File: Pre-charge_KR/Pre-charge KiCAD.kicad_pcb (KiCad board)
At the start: 2 copper layers, 62.9 x 86.1 mm, 60 parts, among them IC1 AL5890-10D-13, IC2 TLV1701AIDBVT, J1 Conn_01x02, J2 Conn_01x06, J3 Conn_01x02, J4 Conn_01x02, K2 G5Q-1A4-DC12, K3 67-1-A-12/2D, Q1 2N7000, Q2 2N7000, Q4 2N7000, U1 HCPL-817-000E, U10 LM7805MPX/NOPB, U13 HCPL-817-000E, U2 LM339N/NOPB, U3 SN74AHCT1G08DBVR, U7 LM741CN/NOPB, U8 SN74AHC1G04DBVRE4

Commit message: precharge complete
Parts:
- removed C11: 0.1uF, FA14_Capacitor:FA18X7R1H104KNU00
- removed C7: 0.22uF, FA14_Capacitor:FA14X7R1H224KNU00
- removed IC1: AL5890-10D-13, AL589010D13:AL589010D13
- removed LED1: LTL-1CHG, LTL1CHG:LTL1CHG
- removed Q1: 2N7000, Package_TO_SOT_THT:TO-92_Inline
- removed R12: 20k, Resistor_THT:R_Axial_DIN0207_L6.3mm_D2.5mm_P10.16mm_Horizontal
- removed R24: 1M, Resistor_THT:R_Axial_DIN0207_L6.3mm_D2.5mm_P10.16mm_Horizontal
- removed R36: 6.8k, Resistor_THT:R_Axial_DIN0207_L6.3mm_D2.5mm_P10.16mm_Horizontal
- removed R37: 4.7k, Resistor_THT:R_Axial_DIN0207_L6.3mm_D2.5mm_P10.16mm_Horizontal
- removed the REF** at (97.4, 35.8)
- removed the REF** at (44.7, 111.9)
- removed the REF** at (97.5, 111.7)
- removed the REF** at (44.6, 35.7)
- removed U10: LM7805MPX/NOPB, Package_TO_SOT_SMD:SOT-223-3_TabPin2
- removed U3: SN74AHCT1G08DBVR, Package_TO_SOT_SMD:SOT-23-5
- removed U7: LM741CN/NOPB, Package_DIP:DIP-8_W7.62mm
- added C5: 2.2uF, FA14_Capacitor:FA14X7R1H224KNU00, F.Cu at (100.9, 70.7)
- added D2: 1N4148, Diode_THT:D_DO-35_SOD27_P7.62mm_Horizontal, F.Cu at (79.9, 57.3)
- added IC3: SN74LVC1G11DCKRE4, SOT65:SOT65P210X110-6N, F.Cu at (85.2, 51.9)
- added IC4: SN74LVC1G08IDCKRQ1, AND:SOT65P210X110-5N, F.Cu at (85.2, 54.9)
- added R10: 56k, Resistor_THT:R_Axial_DIN0411_L9.9mm_D3.6mm_P12.70mm_Horizontal, F.Cu at (76.9, 33.3)
- added R3: 100k, Resistor_THT:R_Axial_DIN0207_L6.3mm_D2.5mm_P10.16mm_Horizontal, F.Cu at (89.4, 52.0)
- added R6: 100k, Resistor_THT:R_Axial_DIN0207_L6.3mm_D2.5mm_P10.16mm_Horizontal, F.Cu at (99.5, 66.1)
- added REF**: MountingHole_3.2mm_M3, MountingHole:MountingHole_3.2mm_M3, F.Cu at (108.2, 86.7)
- added REF**: MountingHole_3.2mm_M3, MountingHole:MountingHole_3.2mm_M3, F.Cu at (108.2, 34.3)
- added REF**: MountingHole_3.2mm_M3, MountingHole:MountingHole_3.2mm_M3, F.Cu at (34.3, 86.7)
- added REF**: MountingHole_3.2mm_M3, MountingHole:MountingHole_3.2mm_M3, F.Cu at (34.2, 34.3)
- C1, C4: value 0.1uF -> 1uF
- C2: value 10uF -> 0.1uF; footprint Capacitor_THT:CP_Radial_D5.0mm_P2.50mm -> FA14_Capacitor:FA18X7R1H104KNU00
- D1: value TZX3V9C-TAP -> 1N4001; footprint Diode_THT:D_DO-35_SOD27_P7.62mm_Horizontal -> Diode_THT:D_DO-41_SOD81_P10.16mm_Horizontal
- D3: value TZX3V0B-TR -> 1N4148
- J3: footprint Phoenix 1x2 Connector:Phoenix_1x2_1729128 -> Connector_JST:JST_XH_B2B-XH-A_1x02_P2.50mm_Vertical
- R1: value 1.5k -> 100k
- R11: value 10k -> 330
- R2: value 1.5k -> 1M
- R32, R33, R7: value 10k -> 100k
- R34: value 180k -> 1.8M
- R35: value 1k -> 2.2k
- R4: value 6.8k -> 10k
- R5: value 4.7k -> 27k
- R8: value 10k -> 56k; footprint Resistor_THT:R_Axial_DIN0207_L6.3mm_D2.5mm_P10.16mm_Horizontal -> Resistor_THT:R_Axial_DIN0411_L9.9mm_D3.6mm_P12.70mm_Horizontal
- R9: value 100 -> 56k; footprint Resistor_THT:R_Axial_DIN0207_L6.3mm_D2.5mm_P10.16mm_Horizontal -> Resistor_THT:R_Axial_DIN0411_L9.9mm_D3.6mm_P12.70mm_Horizontal
- U2: value LM339N/NOPB -> MCP1703AT-3302E/MBVAO; footprint LM339N:DIP794W53P254L1930H508Q14N -> Package_TO_SOT_SMD:SOT-89-3
- U8: value SN74AHC1G04DBVRE4 -> SN74LVC1G04QDBVRQ1
- moved U1 82.8 mm to (105.4, 41.0), turned to -90 degrees
- moved J3 72.4 mm to (43.1, 51.0)
- moved R2 72.3 mm to (46.2, 88.5), turned to 0 degrees
- moved R9 62.4 mm to (65.4, 33.6)
- moved R29 62.2 mm to (92.8, 85.0), turned to 0 degrees
- moved C3 59.9 mm to (40.7, 63.5), turned to 0 degrees
- moved R33 57.6 mm to (102.9, 78.3), turned to 180 degrees
- moved R11 57.4 mm to (76.4, 37.7)
- moved Q2 56.8 mm to (43.2, 58.8), turned to 180 degrees
- moved U13 51.0 mm to (86.4, 78.9), turned to 90 degrees
- moved R27 50.8 mm to (47.0, 71.4)
- moved PS1 49.6 mm to (43.1, 68.3), turned to -90 degrees
- moved R32 48.1 mm to (92.8, 81.7), turned to 0 degrees
- moved R28 45.1 mm to (76.8, 83.1), turned to 0 degrees
- moved C4 45.0 mm to (47.4, 49.5), turned to 0 degrees
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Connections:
- C1 pad 1: 12V_HV -> 3.3V
- C1 pad 2: TS- -> GLV-
- C10 pad 1: 5V -> 3.3V
- C14 pad 1: 5V -> 3.3V
- C2 pad 1: Precharge NOT done -> 3.3V
- C4 pad 1: GLV- -> GLV+
- C4 pad 2: GLV+ -> GLV-
- D1 pad 1: 3V9 -> SDWN_PC
- D1 pad 2: GLV- -> Net-(D1-A)
- D3 pad 1: 3Vref -> Net-(D3-K)
- D3 pad 2: GLV- -> TS-
- J2 pad 1: Precharge_ON -> Shutdown_AIR1+
- J2 pad 3: Shutdown_AIR1+ -> GLV-
- J2 pad 4: Precharge_done/Close_AIR1 -> Precharge_done
- J2 pad 5: TS_activate -> Precharge_EN
- J2 pad 6: GLV- -> Precharge_ON
- K3 pad 3: Net-(Q4-D) -> Net-(D1-A)
- Q4 pad 2: Precharge NOT done -> Net-(D2-K)
- Q4 pad 3: Net-(Q4-D) -> Net-(D1-A)
- R1 pad 1: GLV+ -> GLV-
- R1 pad 2: 3V9 -> Precharge_done
- R11 pad 1: Net-(Q1-G) -> Net-(D3-K)
- R11 pad 2: Precharge_done/Close_AIR1 -> Net-(R10-Pad2)
- R13 pad 2: Net-(R12-Pad1) -> Net-(IC3-B)
- R2 pad 1: GLV+ -> Net-(IC2-IN+)
- R2 pad 2: 3Vref -> Net-(IC2-OUT)
- R28 pad 2: Net-(U7-+) -> Net-(R28-Pad2)
- R29 pad 1: Net-(U7-+) -> Net-(R28-Pad2)
- R30 pad 2: Net-(IC2-IN+) -> Net-(IC2-IN-)
- R31 pad 1: Net-(IC2-IN+) -> Net-(IC2-IN-)
- R32 pad 1: Net-(U7--) -> Net-(R28-Pad2)
- R32 pad 2: Net-(IC2-IN-) -> Net-(IC2-IN+)
- R33 pad 1: Net-(IC2-IN-) -> Net-(IC2-IN+)
- R35 pad 1: Net-(IC2-OUT) -> Net-(R35-Pad1)
- R4 pad 1: Net-(R4-Pad1) -> Net-(IC2-OUT)
- R4 pad 2: Net-(U2A-+) -> 12V_HV
- R5 pad 1: Net-(U2A-+) -> Net-(IC3-B)
- R5 pad 2: GLV- -> SDWN_PC
- R7 pad 1: Precharge_ON -> GLV-
- R7 pad 2: 3V9 -> Net-(D2-K)
- R8 pad 1: Net-(Q1-D) -> PRE_RESIST+
- R8 pad 2: 3V9 -> Net-(R8-Pad2)
- R9 pad 1: Net-(Q1-G) -> Net-(R8-Pad2)
- R9 pad 2: TS_activate -> Net-(R10-Pad1)
- U1 pad 1: Net-(LED1-K) -> Net-(D3-K)
- U1 pad 2: Net-(IC1-IN) -> TS-
- U1 pad 3: Net-(R4-Pad1) -> Precharge_ON
- U1 pad 4: GLV+ -> 3.3V
- U13 pad 1: Net-(IC2-OUT) -> Net-(R35-Pad1)
- U13 pad 2: TS- -> Net-(IC2-OUT)
- U13 pad 3: Net-(R36-Pad2) -> Precharge_done
- U13 pad 4: GLV+ -> 3.3V
- U2 pad 2: Precharge_ON -> GLV+
- U2 pad 3: GLV+ -> 3.3V
- U8 pad 2: Precharge_done/Close_AIR1 -> Precharge_done
- U8 pad 4: Net-(R24-Pad1) -> Precharge NOT done
- U8 pad 5: 5V -> 3.3V
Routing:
- net TS+: track 20.6 -> 144.8 mm
- net GLV+: track 170.2 -> 52.0 mm, vias 1 -> 0
- net TS-: track 49.2 -> 149.3 mm
- net 3.3V: track 0.00 -> 93.9 mm, vias 0 -> 1
- net PRE_RESIST+: track 28.4 -> 113.5 mm
- net Precharge_done/Close_AIR1: track 66.8 -> 0.00 mm, vias 1 -> 0
- net Precharge_ON: track 61.5 -> 9.76 mm, vias 1 -> 0
- net Net-(Q1-D): track 49.8 -> 0.00 mm
- net Net-(R12-Pad1): track 49.6 -> 0.00 mm, vias 1 -> 0
- net 5V: track 49.2 -> 0.00 mm, vias 1 -> 0
- net Net-(IC2-IN+): track 23.3 -> 70.5 mm, vias 0 -> 1
- net Net-(R4-Pad1): track 41.1 -> 0.00 mm
- net Precharge_done: track 0.00 -> 40.3 mm, vias 0 -> 1
- net GLV-: track 39.5 -> 0.00 mm
- net Net-(D2-K): track 0.00 -> 39.1 mm, vias 0 -> 1
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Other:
- board size 62.9 x 86.1 mm -> 88.7 x 61.1 mm
- board text added: "HV"
- board text added: "LV"

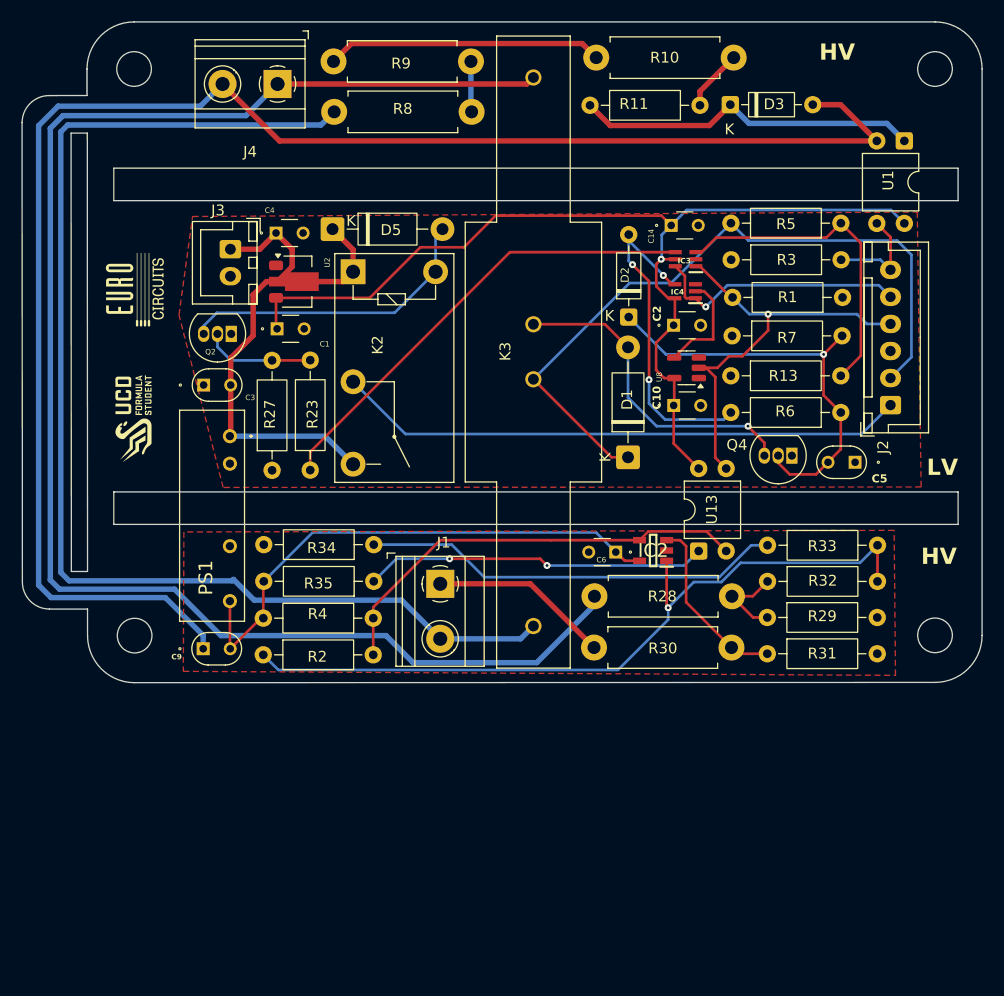
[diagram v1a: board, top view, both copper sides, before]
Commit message: precharge and discharge fixed
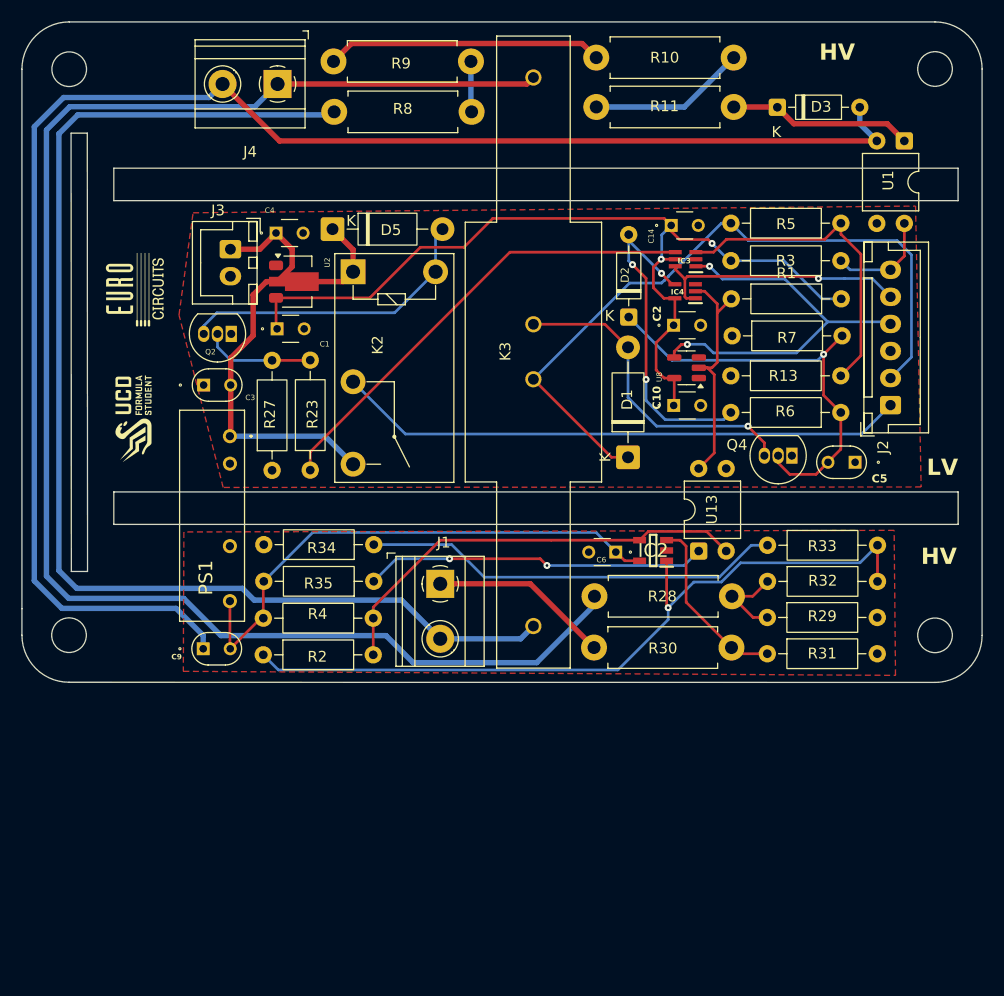
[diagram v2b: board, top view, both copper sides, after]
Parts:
- R1, R3: value 100k -> 10k
- R11: value 330 -> 56k; footprint Resistor_THT:R_Axial_DIN0207_L6.3mm_D2.5mm_P10.16mm_Horizontal -> Resistor_THT:R_Axial_DIN0411_L9.9mm_D3.6mm_P12.70mm_Horizontal
- moved R1 10.3 mm to (89.4, 55.6), turned to 0 degrees
- moved R3 10.1 mm to (99.5, 52.0), turned to 180 degrees
- moved REF** 6.06 mm to (28.2, 86.7)
- moved REF** 6.00 mm to (28.2, 34.4)
- moved D3 4.35 mm to (93.7, 37.9)
- moved R11 0.60 mm to (77.0, 37.9)
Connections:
- J2 pad 6: Precharge_ON -> Precharge_ON_N
- R1 pad 1: GLV- -> Precharge NOT done
- R1 pad 2: Precharge_done -> 3.3V
- R11 pad 1: Net-(D3-K) -> Net-(R10-Pad2)
- R11 pad 2: Net-(R10-Pad2) -> Net-(D3-K)
- R3 pad 1: GLV- -> Precharge_ON_N
- R3 pad 2: Precharge_ON -> 3.3V
- U1 pad 3: Precharge_ON -> GLV-
- U1 pad 4: 3.3V -> Precharge_ON_N
- U13 pad 3: Precharge_done -> GLV-
- U13 pad 4: 3.3V -> Precharge NOT done
- U8 pad 2: Precharge_done -> Precharge NOT done
- U8 pad 4: Precharge NOT done -> Precharge_done
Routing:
- net Net-(D3-K): track 32.0 -> 17.1 mm
- net Precharge NOT done: track 9.89 -> 22.6 mm
- net 3.3V: track 93.9 -> 83.6 mm, vias 1 -> 2
- net Precharge_ON: track 9.76 -> 0.00 mm
- net Precharge_ON_N: track 0.00 -> 9.75 mm
- net Net-(R10-Pad2): track 5.70 -> 14.6 mm
- net Precharge_done: track 40.3 -> 36.7 mm, vias 1 -> 2
- net TS-: track 149.3 -> 146.3 mm
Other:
- board size 88.7 x 61.1 mm -> 88.7 x 61 mm

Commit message: Voltage measurement completed
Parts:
- R4: value 10k -> 100k
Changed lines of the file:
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@@
 			)
 		)
-		(property "Value" "10k"
+		(property "Value" "100k"
 			(at 5.08 2.37 0)
 			(layer "F.Fab")
@@
 			)
 		)
-		(property "Part Number" "MCF 0.25W 10k"
+		(property "Part Number" "MCF 0.25W 100k"
 			(at 0 0 180)
 			(unlocked yes)

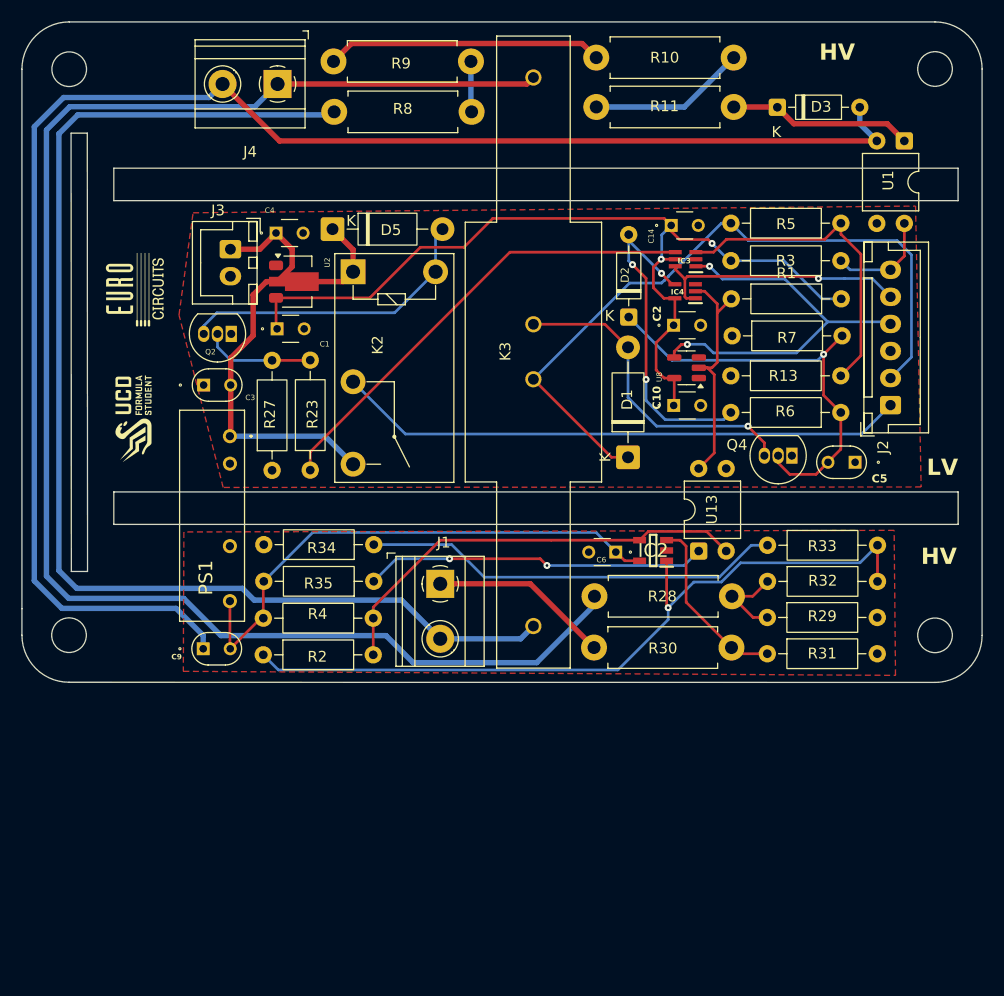
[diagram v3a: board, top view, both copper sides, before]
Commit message: slave with new fuses added
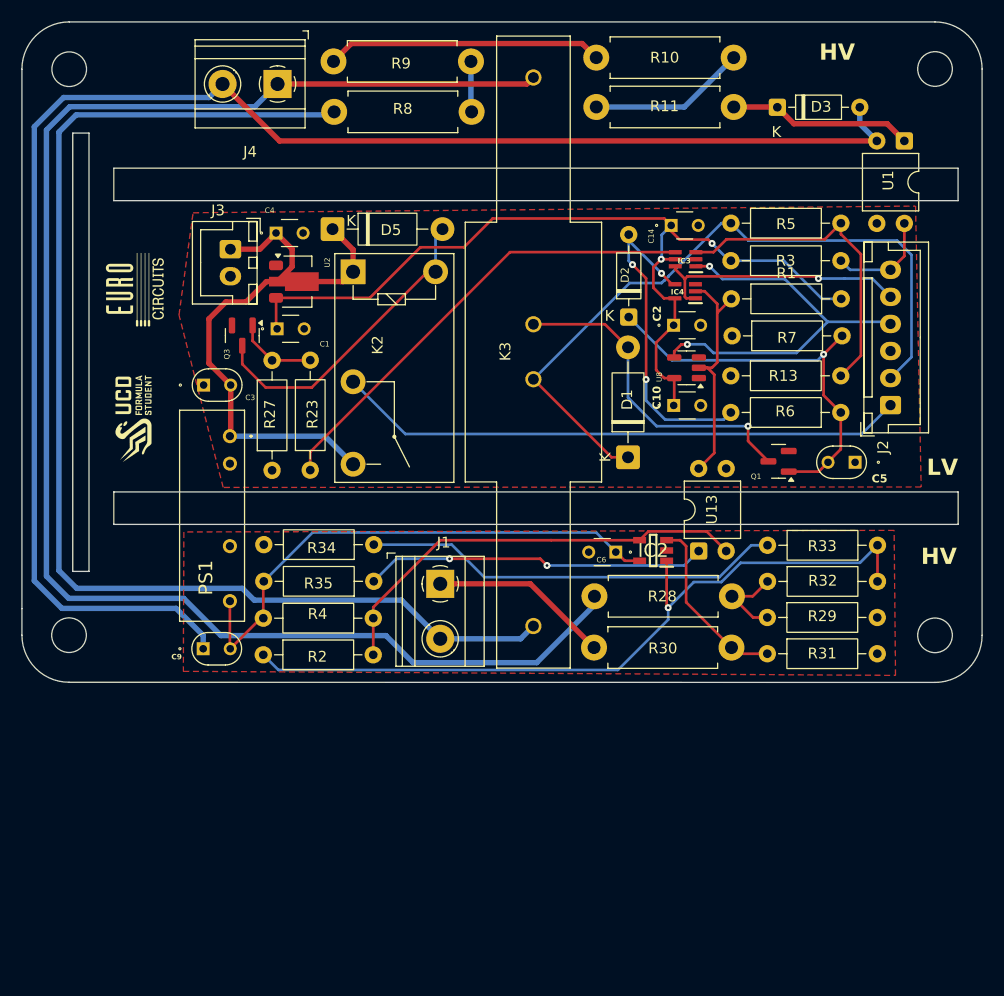
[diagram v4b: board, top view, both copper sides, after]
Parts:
- removed Q2, Q4: 2N7000, Package_TO_SOT_THT:TO-92_Inline
- added Q1: 2N7002, Package_TO_SOT_SMD:SOT-23, F.Cu at (93.8, 70.6)
- added Q3: 2N7002, Package_TO_SOT_SMD:SOT-23, F.Cu at (44.2, 59.0)
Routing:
- net Net-(Q3-G): track 10.3 -> 7.51 mm
- net GLV+: track 52.0 -> 54.8 mm
- net Net-(D2-K): track 39.6 -> 37.4 mm
- net Net-(D1-A): track 29.8 -> 30.5 mm
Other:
- outline, holes or cut-outs redrawn

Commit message: Slave with SMD and no other fuses
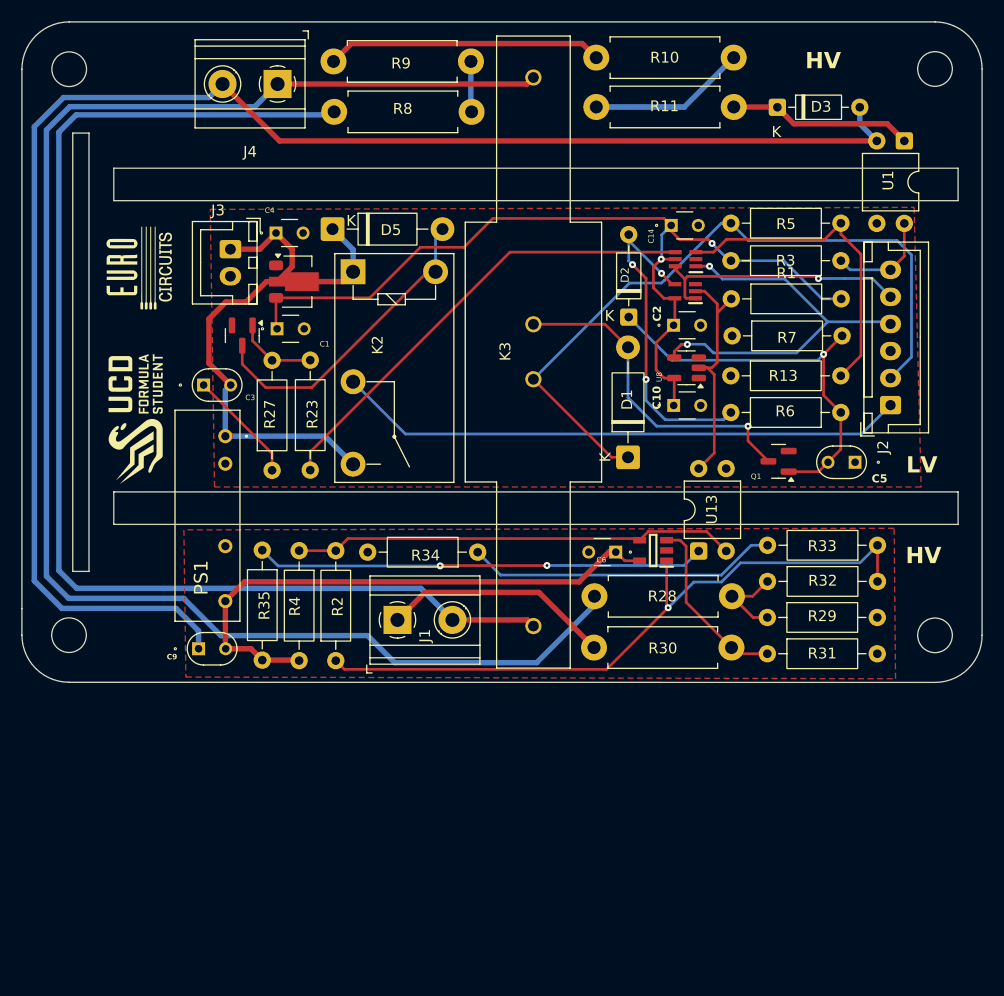
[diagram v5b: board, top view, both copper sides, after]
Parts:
- added G***: LOGO, LOGO, F.Cu at (34.9, 52.7)
- added G***: LOGO, LOGO, F.Cu at (34.4, 66.7)
- moved R35 10.7 mm to (46.1, 78.8), turned to -90 degrees
- moved R34 9.63 mm to (66.0, 79.0)
- moved R4 9.27 mm to (49.5, 78.8), turned to -90 degrees
- moved R2 6.72 mm to (52.9, 89.0), turned to 90 degrees
- moved J1 5.17 mm to (58.6, 85.2), turned to 0 degrees
- moved C9 0.43 mm to (40.2, 87.9)
- moved PS1 0.43 mm to (42.7, 68.3)
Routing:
- net GLV-: track 0.00 -> 10.5 mm
- net Net-(R33-Pad2): track 38.8 -> 28.8 mm
- net Net-(R35-Pad1): track 31.7 -> 41.5 mm
- net Net-(IC2-IN+): track 70.5 -> 62.9 mm
- net PRE_RESIST-: track 16.6 -> 21.3 mm
- net 12V_HV: track 49.7 -> 52.2 mm
- net PRE_RESIST+: track 113.7 -> 112.7 mm
- net GLV+: track 54.8 -> 55.5 mm
